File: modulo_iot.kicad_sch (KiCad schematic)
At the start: 46 parts, among them J1 SMA_CONNECTOR, Q2 BC817, Q3 BC817, Q4 BC817, Q5 BC817, Q6 BC817, Q7 BC817, Q8 BC817, U6 BG95-M3

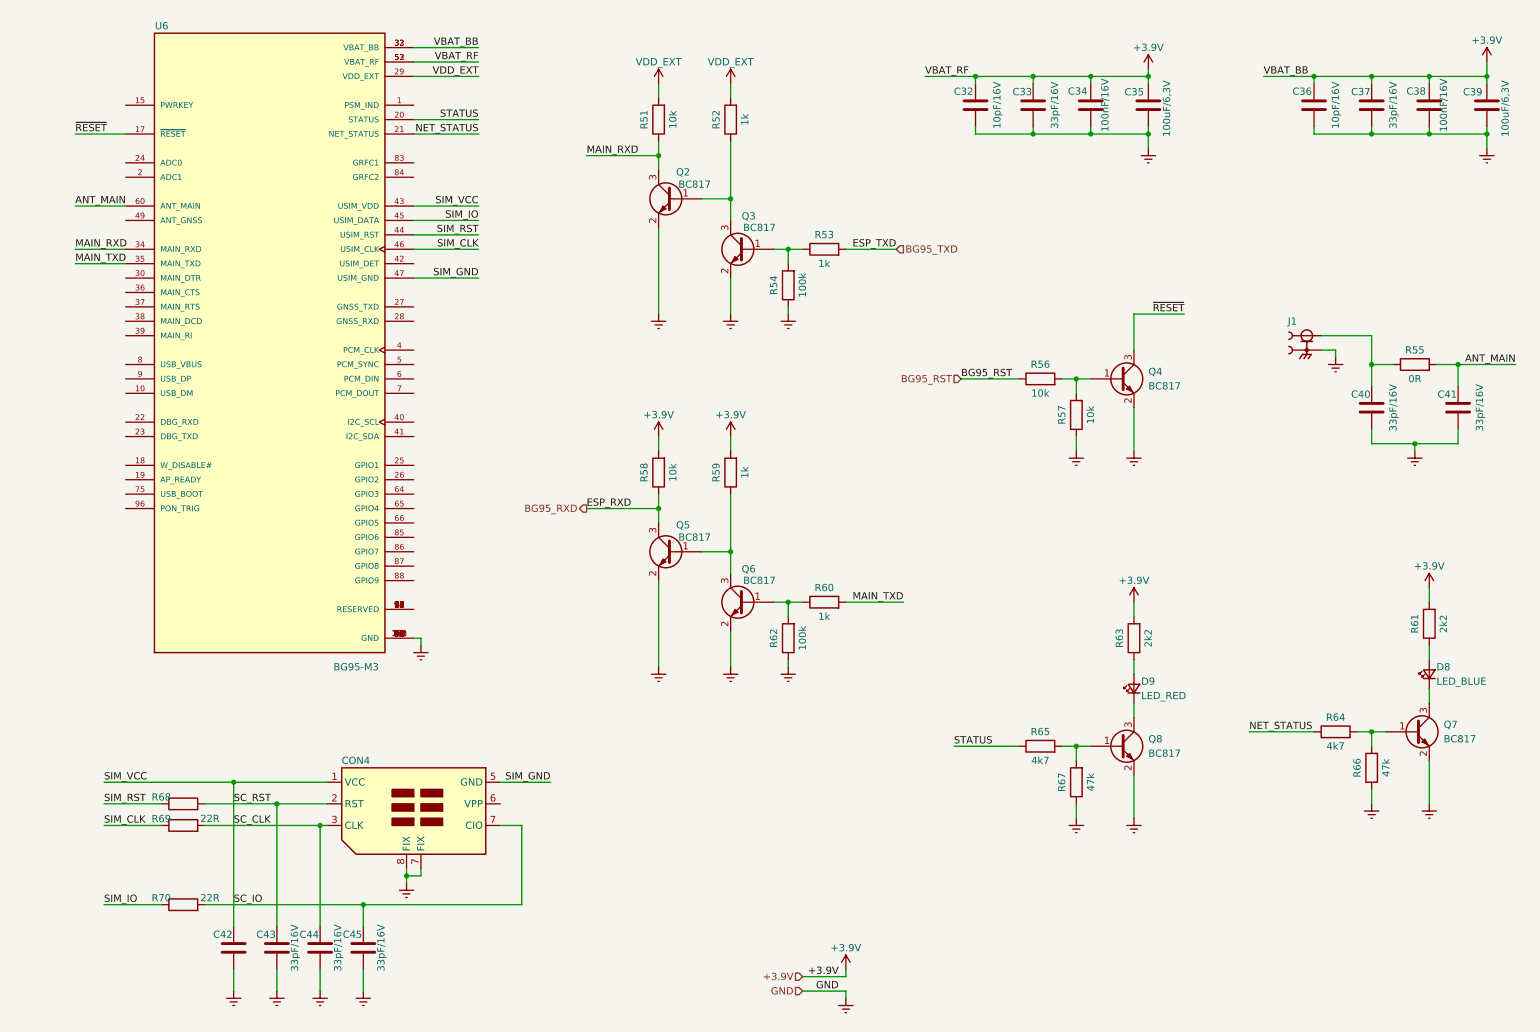
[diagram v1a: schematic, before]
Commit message: Continuando a adição dos hierarchical labels
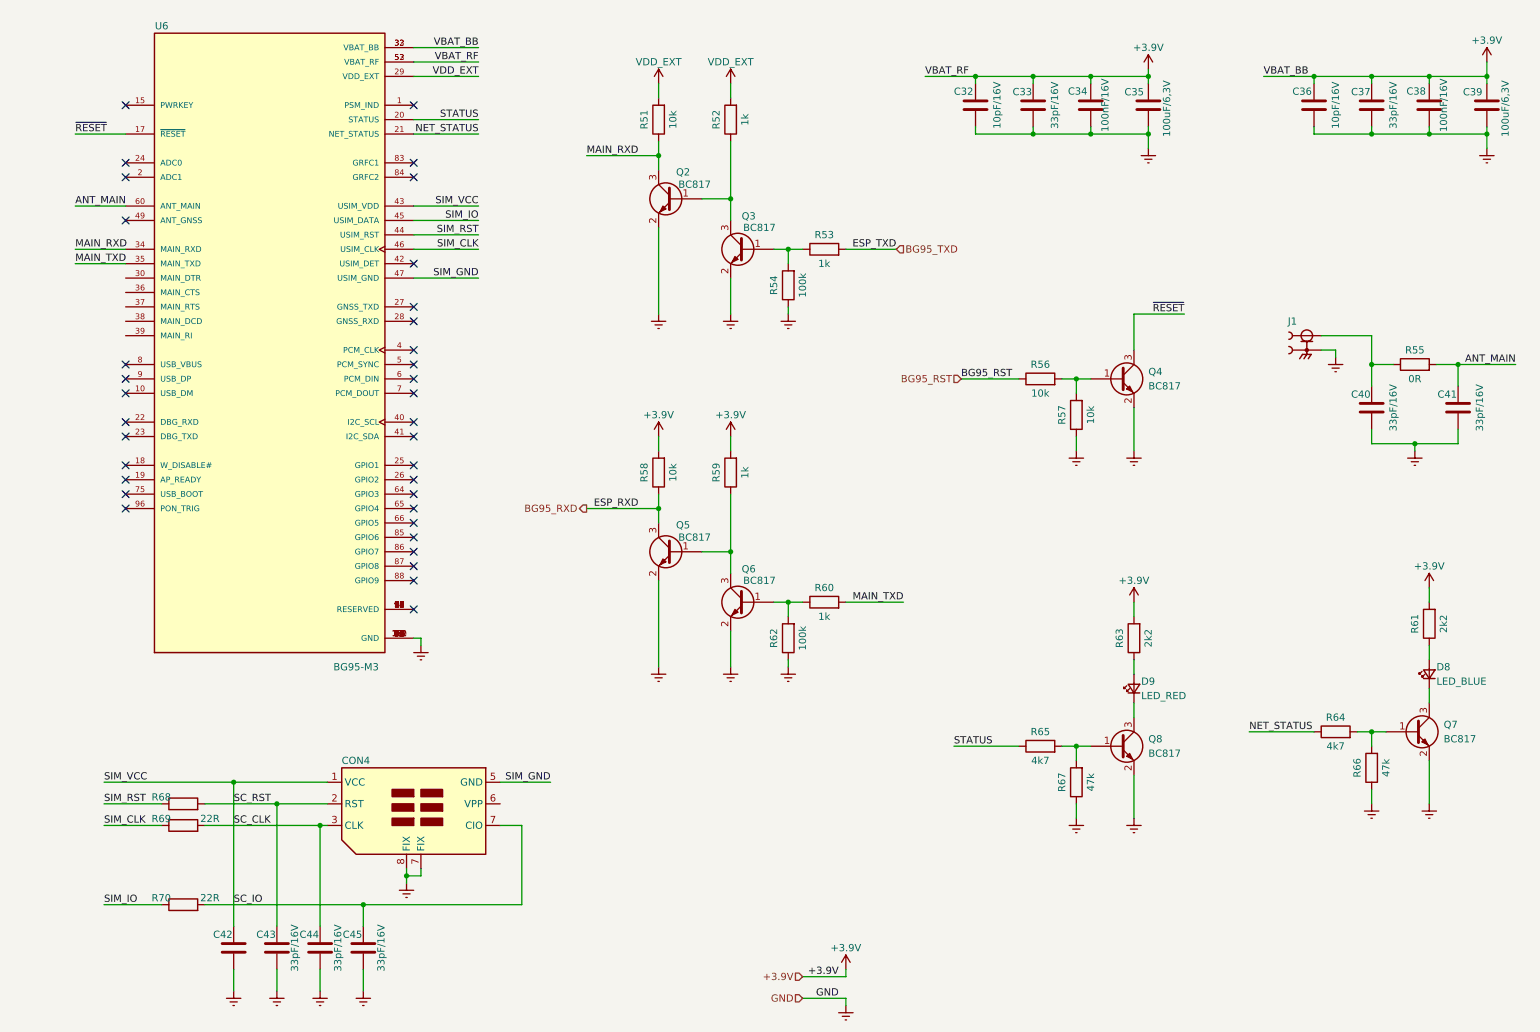
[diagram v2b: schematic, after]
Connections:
- no-connect marks 0 -> 35
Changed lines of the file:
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@@
   (junction (at 212.09 25.4) (diameter 0) (color 0 0 0 0)
   )
+  (no_connect (at 31.75 30.48))
+  (no_connect (at 82.55 68.58))
+  (no_connect (at 82.55 66.04))
+  (no_connect (at 82.55 58.42))
+  (no_connect (at 31.75 50.8))
+  (no_connect (at 31.75 76.2))
+  (no_connect (at 31.75 78.74))
+  (no_connect (at 31.75 81.28))
+  (no_connect (at 31.75 101.6))
+  (no_connect (at 82.55 81.28))
+  (no_connect (at 82.55 86.36))
+  (no_connect (at 82.55 88.9))
+  (no_connect (at 82.55 40.64))
+  (no_connect (at 82.55 43.18))
+  (no_connect (at 82.55 73.66))
+  (no_connect (at 82.55 76.2))
+  (no_connect (at 82.55 78.74))
+  (no_connect (at 31.75 40.64))
+  (no_connect (at 31.75 43.18))
+  (no_connect (at 82.55 30.48))
+  (no_connect (at 82.55 93.98))
+  (no_connect (at 82.55 96.52))
+  (no_connect (at 82.55 99.06))
+  (no_connect (at 82.55 101.6))
+  (no_connect (at 82.55 119.38))
+  (no_connect (at 82.55 104.14))
+  (no_connect (at 82.55 106.68))
+  (no_connect (at 82.55 109.22))
+  (no_connect (at 82.55 111.76))
+  (no_connect (at 82.55 114.3))
+  (no_connect (at 31.75 86.36))
+  (no_connect (at 31.75 88.9))
+  (no_connect (at 31.75 93.98))
+  (no_connect (at 31.75 96.52))
+  (no_connect (at 31.75 99.06))
   (wire (pts (xy 251.46 34.29) (xy 251.46 35.56))
     (stroke (width 0) (type default) (color 0 0 0 0))
@@
     (stroke (width 0) (type default) (color 0 0 0 0))
   )
-  (wire (pts (xy 158.75 186.69) (xy 158.75 187.96))
+  (wire (pts (xy 158.75 187.96) (xy 158.75 189.23))
     (stroke (width 0) (type default) (color 0 0 0 0))
   )
@@
     (stroke (width 0) (type default) (color 0 0 0 0))
   )
-  (wire (pts (xy 151.13 186.69) (xy 158.75 186.69))
+  (wire (pts (xy 151.13 187.96) (xy 158.75 187.96))
     (stroke (width 0) (type default) (color 0 0 0 0))
   )
@@
     (effects (font (size 1.27 1.27)) (justify left bottom))
   )
-  (label "GND" (at 157.48 186.69 180)
+  (label "GND" (at 157.48 187.96 180)
     (effects (font (size 1.27 1.27)) (justify right bottom))
   )
@@
     (effects (font (size 1.27 1.27)) (justify right bottom))
   )
-  (label "ESP_RXD" (at 113.03 101.6 0)
+  (label "ESP_RXD" (at 114.3 101.6 0)
     (effects (font (size 1.27 1.27)) (justify left bottom))
   )
@@
     (effects (font (size 1.27 1.27)) (justify right))
   )
-  (hierarchical_label "GND" (shape input) (at 151.13 186.69 180)
+  (hierarchical_label "GND" (shape input) (at 151.13 187.96 180)
     (effects (font (size 1.27 1.27)) (justify right))
   )
@@
     (pin "1")
   )
-  (symbol (lib_id "power:GNDREF") (at 158.75 187.96 0) (unit 1)
+  (symbol (lib_id "power:GNDREF") (at 158.75 189.23 0) (unit 1)
     (in_bom yes) (on_board yes) (fields_autoplaced)
-    (property "Reference" "#PWR0109" (id 0) (at 158.75 194.31 0)
-      (effects (font (size 1.27 1.27)) hide)
-    )
-    (property "Value" "GNDREF" (id 1) (at 158.75 193.04 0)
-      (effects (font (size 1.27 1.27)) hide)
-    )
-    (property "Footprint" "" (id 2) (at 158.75 187.96 0)
-      (effects (font (size 1.27 1.27)) hide)
-    )
-    (property "Datasheet" "" (id 3) (at 158.75 187.96 0)
-      (effects (font (size 1.27 1.27)) hide)
-    )
+    (property "Reference" "#PWR0109" (id 0) (at 158.75 195.58 0)
+      (effects (font (size 1.27 1.27)) hide)
+    )
+    (property "Value" "GNDREF" (id 1) (at 158.75 194.31 0)
+      (effects (font (size 1.27 1.27)) hide)
+    )
+    (property "Footprint" "" (id 2) (at 158.75 189.23 0)
+      (effects (font (size 1.27 1.27)) hide)
+    )
+    (property "Datasheet" "" (id 3) (at 158.75 189.23 0)
+      (effects (font (size 1.27 1.27)) hide)
+    )

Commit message: Inserido encapsulamento 0603 para os resistores
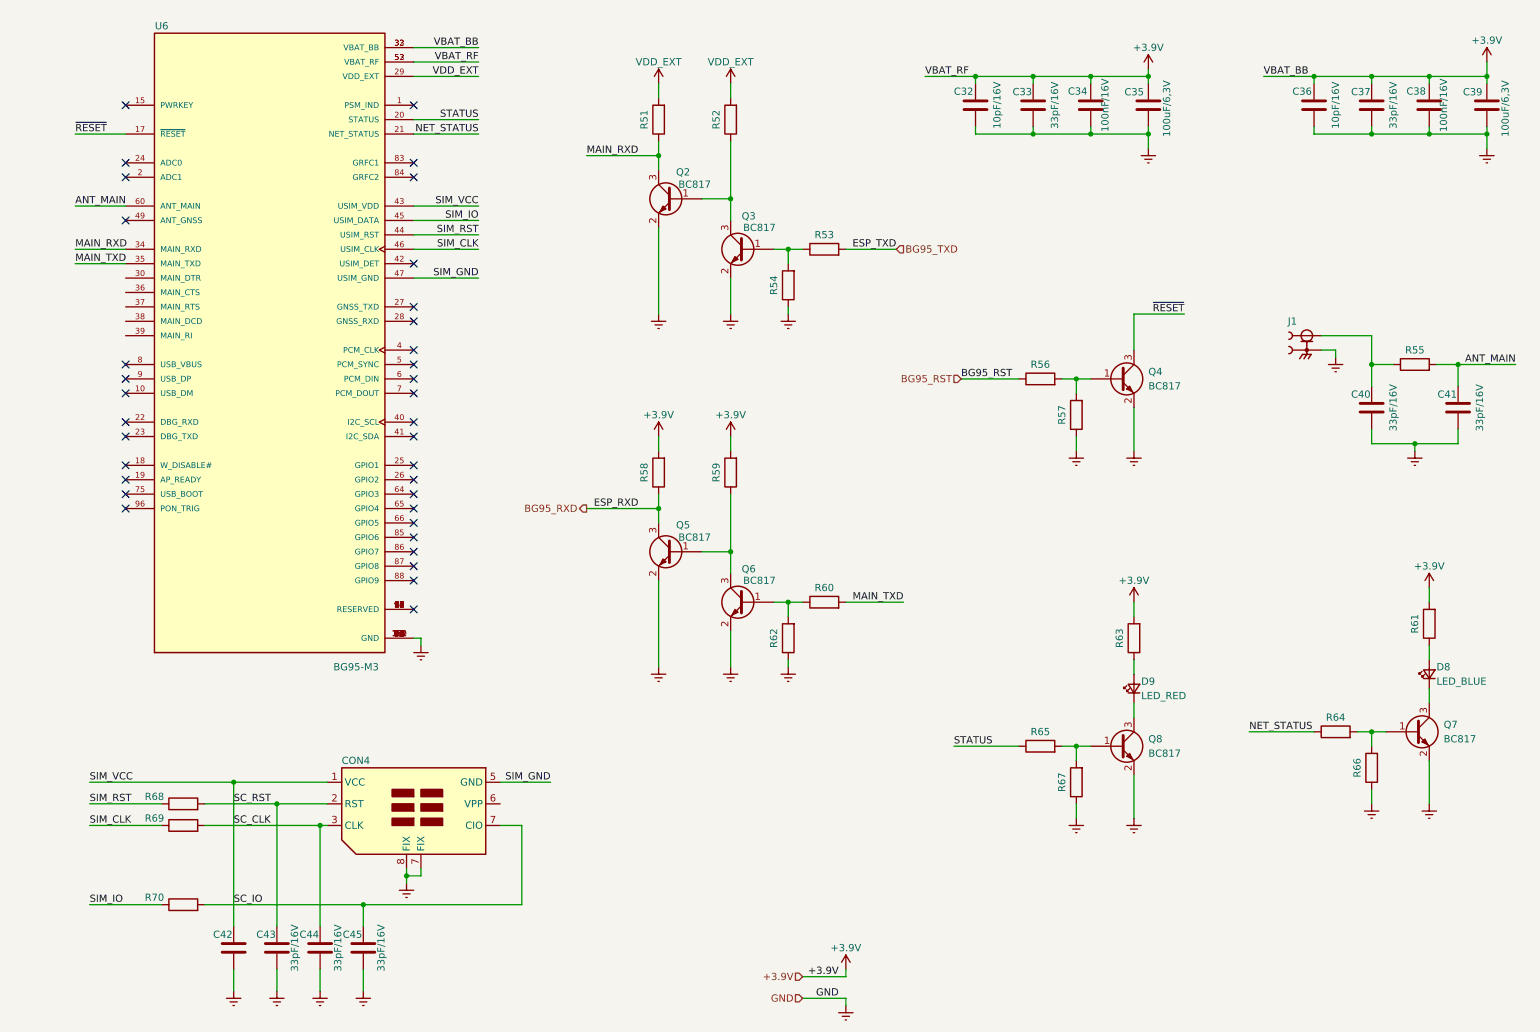
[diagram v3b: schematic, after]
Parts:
- R51, R56, R57, R58: value 10k -> (none); footprint Resistor_SMD:R_0402_1005Metric_Pad0.72x0.64mm_HandSolder -> (none)
- R52, R53, R59, R60: value 1k -> (none); footprint Resistor_SMD:R_0402_1005Metric_Pad0.72x0.64mm_HandSolder -> (none)
- R54, R62: value 100k -> (none); footprint Resistor_SMD:R_0402_1005Metric_Pad0.72x0.64mm_HandSolder -> (none)
- R55: value 0R -> (none); footprint Resistor_SMD:R_0402_1005Metric_Pad0.72x0.64mm_HandSolder -> (none)
- R61, R63: value 2k2 -> (none); footprint Resistor_SMD:R_0402_1005Metric_Pad0.72x0.64mm_HandSolder -> (none)
- R64, R65: value 4k7 -> (none); footprint Resistor_SMD:R_0402_1005Metric_Pad0.72x0.64mm_HandSolder -> (none)
- R66, R67: value 47k -> (none); footprint Resistor_SMD:R_0402_1005Metric_Pad0.72x0.64mm_HandSolder -> (none)
- R68: footprint Resistor_SMD:R_0402_1005Metric_Pad0.72x0.64mm_HandSolder -> (none)
- R69, R70: value 22R -> (none); footprint Resistor_SMD:R_0402_1005Metric_Pad0.72x0.64mm_HandSolder -> (none)

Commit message: Corrigido alguns ERC e adicionado circuito DTR e RI do BG95
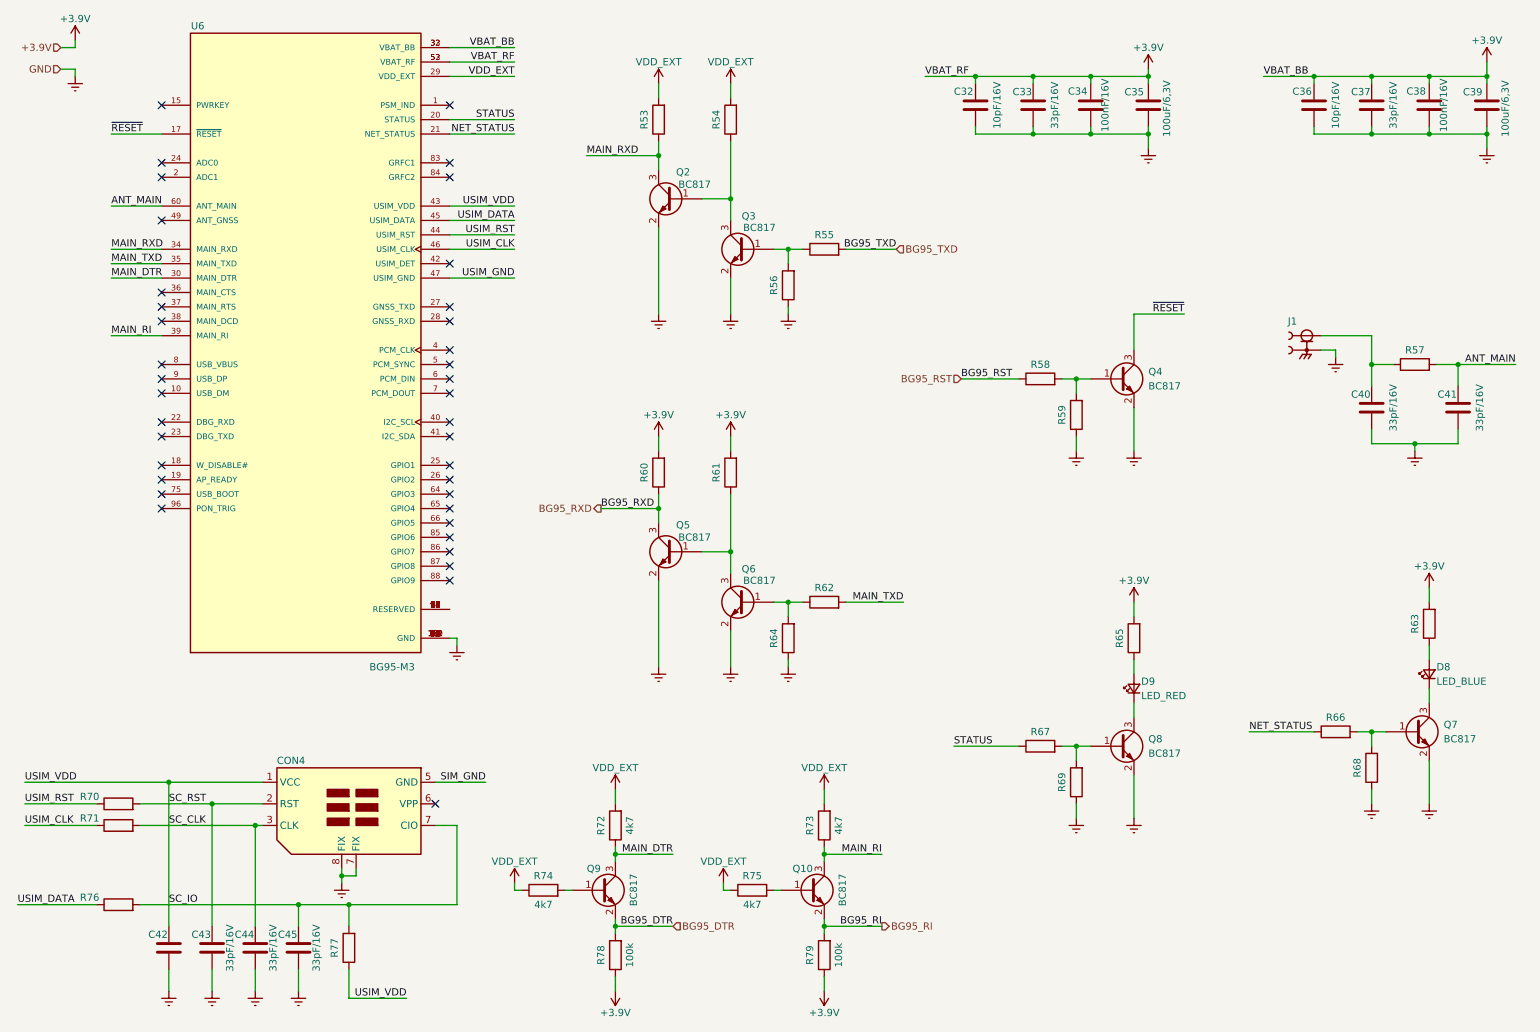
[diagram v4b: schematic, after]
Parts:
- added Q10, Q9: BC817, Package_TO_SOT_SMD:SOT-23, symbol Transistor_BJT:BC817
- added R72, R73, R74, R75: 4k7, Resistor_SMD:R_0603_1608Metric_Pad0.98x0.95mm_HandSolder, symbol Device:R
- added R77: (no value), symbol Device:R
- added R78, R79: 100k, Resistor_SMD:R_0603_1608Metric_Pad0.98x0.95mm_HandSolder, symbol Device:R
- renumbered R51 to R53, R52 to R54, R53 to R55, R54 to R56, R55 to R57, R56 to R58, R57 to R59, R58 to R60, R59 to R61, R60 to R62, R61 to R63, R62 to R64, R63 to R65, R64 to R66, R65 to R67, R66 to R68, R67 to R69, R68 to R70, R69 to R71, R70 to R76
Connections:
- net SC_CLK: now also R77.1, R77.2
- net SIM_GND: no longer U6.47 (USIM_GND)
- net MAIN_DTR: now reaches U6.30 (MAIN_DTR)
- net MAIN_DTR: now also Q9.3 (C), R72.1
- net MAIN_RI: now reaches U6.39 (MAIN_RI)
- net MAIN_RI: now also Q10.3 (C), R73.1
- net SIM_CLK renamed USIM_CLK
- net SIM_IO renamed USIM_DATA
- net SIM_RST renamed USIM_RST
- new net: Q9.1 (B), R74.2
- new net: Q10.1 (B), R75.2
- new net BG95_DTR: Q9.2 (E), R78.2
- new net BG95_RI: Q10.2 (E), R79.2
- new net USIM_GND: U6.47 (USIM_GND)
- no-connect marks 35 -> 38
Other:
- moved on the sheet: C42, C43, C44, C45, CON4, R70, R71, R76, U6

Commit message: Correções de ECR-Electrical Rules Checker
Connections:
- net GNDREF renamed GND
- removed net SC_CLK: C42.2, C43.2, C44.2, C45.2, CON4.1 (VCC), CON4.2 (RST), CON4.3 (CLK), CON4.7 (FIX), R70.2, R71.2, R76.2, R77.1, R77.2, U6.43 (USIM_VDD)
- new net: C45.2, CON4.7 (FIX), R76.2, R77.2
- new net: C44.2, CON4.3 (CLK), R71.2
- new net: C43.2, CON4.2 (RST), R70.2
- new net USIM_VDD: C42.2, CON4.1 (VCC), R77.1, U6.43 (USIM_VDD)
